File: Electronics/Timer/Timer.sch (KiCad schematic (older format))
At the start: 24 parts, among them J1 RJ10, U1 MIC5504-3.3YM5, U2 74HC165

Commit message: Updated boards for two-sided manufacture.
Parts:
- C1, C2, C3, C4, C5: symbol Device:C -> Timer-rescue:C-Device
- D1: footprint Diodes_SMD:D_SOD-123 -> Diode_SMD:D_SMA_Handsoldering; symbol Device:D_Schottky -> Timer-rescue:D_Schottky-Device
- D2: symbol Device:LED -> Timer-rescue:LED-Device
- D3, D4: symbol Device:D_Zener -> Timer-rescue:D_Zener-Device
- J1: symbol Connector:RJ10 -> Timer-rescue:RJ10-Connector
- R1, R2, R3, R4, R5, R6: symbol Device:R -> Timer-rescue:R-Device
- RN1: symbol Device:R_Network05 -> Timer-rescue:R_Network05-Device
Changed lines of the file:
@@
 EESchema Schematic File Version 4
-LIBS:Timer-cache
-EELAYER 26 0
+EELAYER 30 0
 EELAYER END
 $Descr A4 11693 8268
@@
 $EndDescr
 $Comp
-L power:GND #PWR01
+L Timer-rescue:GND-power #PWR01
 U 1 1 5B2D833C
 P 1450 1550
@@
 $EndComp
 $Comp
-L power:PWR_FLAG #FLG02
+L Timer-rescue:PWR_FLAG-power #FLG02
 U 1 1 5B2D8350
 P 1450 1500
@@
 $EndComp
 $Comp
-L Device:R_Network05 RN1
+L Timer-rescue:R_Network05-Device RN1
 U 1 1 5B2D83AE
 P 9100 1100
@@
 $EndComp
 $Comp
-L Device:LED D2
+L Timer-rescue:LED-Device D2
 U 1 1 5B2D9078
 P 3600 3700
@@
 $EndComp
 $Comp
-L power:+3.3V #PWR03
+L Timer-rescue:+3.3V-power #PWR03
 U 1 1 5B2D91A7
 P 6300 3700
@@
 $EndComp
 $Comp
-L power:GND #PWR04
+L Timer-rescue:GND-power #PWR04
 U 1 1 5B2D939C
 P 2000 3600
@@
 NoConn ~ 8300 1550
 $Comp
-L power:GND #PWR05
+L Timer-rescue:GND-power #PWR05
 U 1 1 5B2D93FE
 P 7700 3250
@@
 $EndComp
 $Comp
-L Device:C C2
+L Timer-rescue:C-Device C2
 U 1 1 5B2D958C
 P 8000 1000
@@
 $EndComp
 $Comp
-L power:GND #PWR06
+L Timer-rescue:GND-power #PWR06
 U 1 1 5B2D95FE
 P 8150 1000
@@
 $EndComp
 $Comp
-L power:+3.3V #PWR07
+L Timer-rescue:+3.3V-power #PWR07
 U 1 1 5B2D9621
 P 7700 950
@@
 NoConn ~ 10400 5350
 $Comp
-L power:GND #PWR08
+L Timer-rescue:GND-power #PWR08
 U 1 1 5B2DA1C3
 P 10400 1950
@@
 $EndComp
 $Comp
-L power:GND #PWR09
+L Timer-rescue:GND-power #PWR09
 U 1 1 5B2DA234
 P 10400 2850
@@
 $EndComp
 $Comp
-L Device:R R1
+L Timer-rescue:R-Device R1
 U 1 1 5B46CBDD
 P 3200 3300
@@
 $EndComp
 $Comp
-L Device:D_Zener D3
+L Timer-rescue:D_Zener-Device D3
 U 1 1 5B46CC66
 P 4250 3600
@@
 $EndComp
 $Comp
-L power:GND #PWR010
+L Timer-rescue:GND-power #PWR010
 U 1 1 5B46CF5B
 P 4250 3850
@@
 $EndComp
 $Comp
-L Device:D_Schottky D1
+L Timer-rescue:D_Schottky-Device D1
 U 1 1 5B5B5DBA
 P 3800 3300
 F 0 "D1" H 3800 3400 50  0000 C CNN
 F 1 "BAT54" H 3800 3200 50  0000 C CNN
-F 2 "Diodes_SMD:D_SOD-123" H 3800 3300 50  0001 C CNN
+F 2 "Diode_SMD:D_SMA_Handsoldering" H 3800 3300 50  0001 C CNN
 F 3 "" H 3800 3300 50  0001 C CNN
 	1    3800 3300
@@
 $EndComp
 $Comp
-L Device:C C1
+L Timer-rescue:C-Device C1
 U 1 1 5B5B6007
 P 4600 3600
@@
 $EndComp
 $Comp
-L Device:R R2
+L Timer-rescue:R-Device R2
 U 1 1 5B5B6D85
 P 3200 3700
@@
 $EndComp
 $Comp
-L power:GND #PWR011
+L Timer-rescue:GND-power #PWR011
 U 1 1 5B5B72D4
 P 6200 4250
@@
 $EndComp
 $Comp
-L power:GND #PWR012
+L Timer-rescue:GND-power #PWR012
 U 1 1 5B5E52E5
 P 4600 3850
@@
 $EndComp
 $Comp
-L power:GND #PWR013
+L Timer-rescue:GND-power #PWR013
 U 1 1 5B5E531A
 P 5350 4250
@@
 $EndComp
 $Comp
-L power:+5V #PWR014
+L Timer-rescue:+5V-power #PWR014
 U 1 1 5B5E5952
 P 5000 3300
@@
 $EndComp
 $Comp
-L power:+5V #PWR015
+L Timer-rescue:+5V-power #PWR015
 U 1 1 5B5E5C2E
 P 5800 3900
@@
 $EndComp
 $Comp
-L Device:D_Zener D4
+L Timer-rescue:D_Zener-Device D4
 U 1 1 5B5E643D
 P 6200 4000
@@
 $EndComp
 $Comp
-L power:GND #PWR016
+L Timer-rescue:GND-power #PWR016
 U 1 1 5B5E67AC
 P 8300 2600
@@
 $EndComp
 $Comp
-L power:GND #PWR018
+L Timer-rescue:GND-power #PWR018
 U 1 1 5B5E6846
 P 7100 1850
@@
 $EndComp
 $Comp
-L power:GND #PWR019
+L Timer-rescue:GND-power #PWR019
 U 1 1 5B5E781E
 P 3850 3700
@@
 $EndComp
 $Comp
-L Device:R R3
+L Timer-rescue:R-Device R3
 U 1 1 5B5E7B1D
 P 3200 4100
@@
 CLK
 $Comp
-L Device:C C3
+L Timer-rescue:C-Device C3
 U 1 1 5B5E8ED0
 P 2400 4400
@@
 $EndComp
 $Comp
-L power:GND #PWR020
+L Timer-rescue:GND-power #PWR020
 U 1 1 5B5E8FC7
 P 2400 4650
@@
 Q
 $Comp
-L Device:R R4
+L Timer-rescue:R-Device R4
 U 1 1 5B5E9AEB
 P 3200 4500
@@
 $EndComp
 $Comp
-L Device:R R5
+L Timer-rescue:R-Device R5
 U 1 1 5B5E9B57
 P 2050 4100
@@
 CLK
 $Comp
-L power:GND #PWR021
+L Timer-rescue:GND-power #PWR021
 U 1 1 5B5EA020
 P 7100 2900
@@
 $EndComp
 $Comp
-L power:GND #PWR022
+L Timer-rescue:GND-power #PWR022
 U 1 1 5B5EA568
 P 10400 3750
@@
 $EndComp
 $Comp
-L power:GND #PWR023
+L Timer-rescue:GND-power #PWR023
 U 1 1 5B5EA5B2
 P 10400 4650
@@
 $EndComp
 $Comp
-L power:GND #PWR024
+L Timer-rescue:GND-power #PWR024
 U 1 1 5B5EA5FC
 P 10400 5550
@@
 $EndComp
 $Comp
-L power:+3.3V #PWR025
+L Timer-rescue:+3.3V-power #PWR025
 U 1 1 5B5E2650
 P 8300 2450
@@
 NoConn ~ 9300 1300
 $Comp
-L Device:R R6
+L Timer-rescue:R-Device R6
 U 1 1 5B5E2B7E
 P 8800 2750
@@
 $EndComp
 $Comp
-L power:+3.3V #PWR026
+L Timer-rescue:+3.3V-power #PWR026
 U 1 1 5B5E2F61
 P 8800 2600
@@
 	9300 4550 8900 4550
 $Comp
-L power:+3.3V #PWR0101
+L Timer-rescue:+3.3V-power #PWR0101
 U 1 1 5B5E304C
 P 8900 900
@@
 	9200 1850 9300 1850
 $Comp
-L power:GND #PWR0102
+L Timer-rescue:GND-power #PWR0102
 U 1 1 5BC0F80F
 P 9300 5000
@@
 $EndComp
 $Comp
-L power:GND #PWR0103
+L Timer-rescue:GND-power #PWR0103
 U 1 1 5BC0F846
 P 9300 5900
@@
 $EndComp
 $Comp
-L power:GND #PWR0104
+L Timer-rescue:GND-power #PWR0104
 U 1 1 5BC0F87D
 P 10400 5100
@@
 $EndComp
 $Comp
-L power:GND #PWR0105
+L Timer-rescue:GND-power #PWR0105
 U 1 1 5BC14F66
 P 10400 4900
@@
 $EndComp
 $Comp
-L power:GND #PWR0106
+L Timer-rescue:GND-power #PWR0106
 U 1 1 5BC17578
 P 10400 5800
@@
 $EndComp
 $Comp
-L power:GND #PWR0107
+L Timer-rescue:GND-power #PWR0107
 U 1 1 5BC175AF
 P 10400 6000
@@
 $EndComp
 $Comp
-L power:GND #PWR0108
+L Timer-rescue:GND-power #PWR0108
 U 1 1 5BC1AEE3
 P 9300 4100
@@
 $EndComp
 $Comp
-L power:GND #PWR0109
+L Timer-rescue:GND-power #PWR0109
 U 1 1 5BC1AF1A
 P 10400 4200
@@
 $EndComp
 $Comp
-L power:GND #PWR0110
+L Timer-rescue:GND-power #PWR0110
 U 1 1 5BC1AF51
 P 10400 4000
@@
 $EndComp
 $Comp
-L power:GND #PWR0111
+L Timer-rescue:GND-power #PWR0111
 U 1 1 5BC1E4A7
 P 10400 3100
@@
 $EndComp
 $Comp
-L power:GND #PWR0112
+L Timer-rescue:GND-power #PWR0112
 U 1 1 5BC1E4DE
 P 10400 3300
@@
 $EndComp
 $Comp
-L power:GND #PWR0113
+L Timer-rescue:GND-power #PWR0113
 U 1 1 5BC1E515
 P 9300 3200
@@
 $EndComp
 $Comp
-L power:GND #PWR0114
+L Timer-rescue:GND-power #PWR0114
 U 1 1 5BC21A81
 P 9300 2300
@@
 $EndComp
 $Comp
-L power:GND #PWR0115
+L Timer-rescue:GND-power #PWR0115
 U 1 1 5BC21AB8
 P 10400 2200
@@
 $EndComp
 $Comp
-L power:GND #PWR0116
+L Timer-rescue:GND-power #PWR0116
 U 1 1 5BC21AEF
 P 10400 2400
@@
 $EndComp
 $Comp
-L Device:C C4
+L Timer-rescue:C-Device C4
 U 1 1 5C3BCA70
 P 6150 1550
@@
 	6150 1400 7100 1400
 $Comp
-L power:GND #PWR0117
+L Timer-rescue:GND-power #PWR0117
 U 1 1 5C3BDD23
 P 6150 1700
@@
 $EndComp
 $Comp
-L Device:C C5
+L Timer-rescue:C-Device C5
 U 1 1 5C3C02A8
 P 6550 1700
@@
 $EndComp
 $Comp
-L power:GND #PWR0118
+L Timer-rescue:GND-power #PWR0118
 U 1 1 5C3C02AF
 P 6550 1850
@@
 	6550 1550 7100 1550
 $Comp
-L Connector:RJ10 J1
+L Timer-rescue:RJ10-Connector J1
 U 1 1 5C3D5B2C
 P 1600 3500
@@
 	8300 2900 8800 2900
 $Comp
-L power:GND #PWR017
+L Timer-rescue:GND-power #PWR017
 U 1 1 5B5E67F9
 P 8300 2750

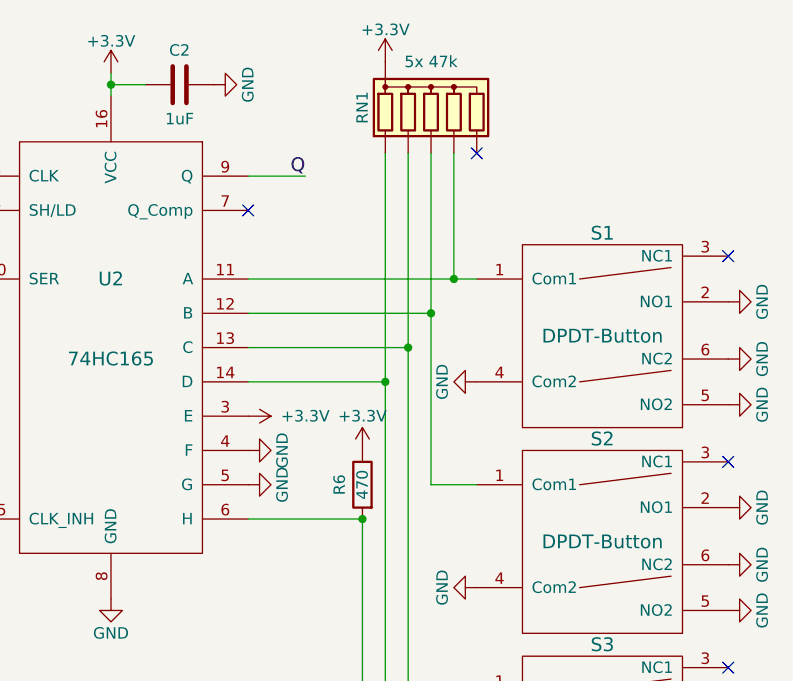
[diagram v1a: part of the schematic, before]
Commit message: Updated component sourcing
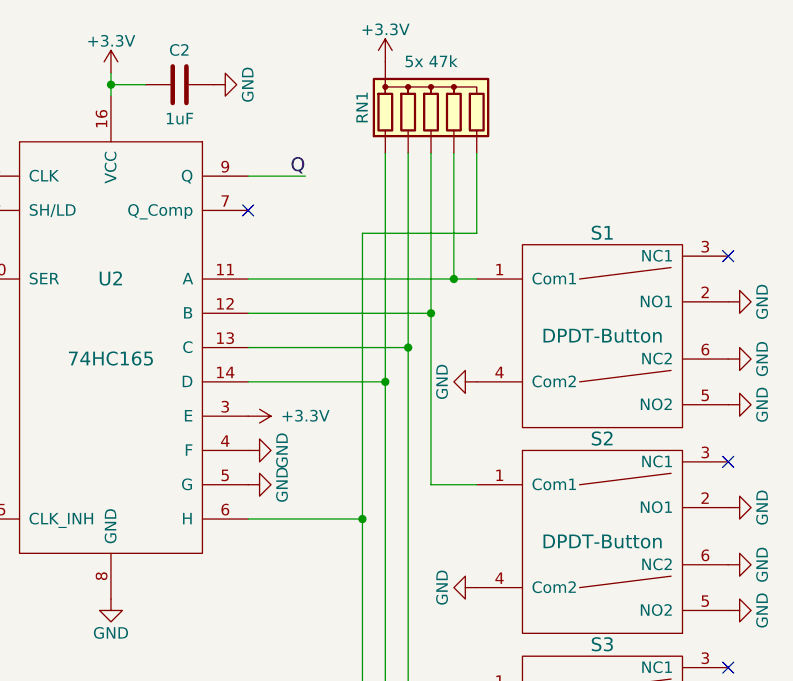
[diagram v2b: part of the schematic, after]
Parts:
- removed R6: 470, Resistors_SMD:R_1206_HandSoldering, symbol Timer-rescue:R-Device
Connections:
- net at RN1.6 (R5): now also S5.1 (Com1), U2.6 (H)
- no-connect marks 7 -> 6
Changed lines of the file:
@@
 Wire Wire Line
 	8800 5450 9300 5450
-NoConn ~ 9300 1300
-$Comp
-L Timer-rescue:R-Device R6
-U 1 1 5B5E2B7E
-P 8800 2750
-F 0 "R6" V 8900 2750 50  0000 C CNN
-F 1 "470" V 8800 2750 50  0000 C CNN
-F 2 "Resistors_SMD:R_1206_HandSoldering" V 8730 2750 50  0001 C CNN
-F 3 "" H 8800 2750 50  0001 C CNN
-	1    8800 2750
-	-1   0    0    -1
-$EndComp
-$Comp
-L Timer-rescue:+3.3V-power #PWR026
-U 1 1 5B5E2F61
-P 8800 2600
-F 0 "#PWR026" H 8800 2450 50  0001 C CNN
-F 1 "+3.3V" H 8800 2750 50  0000 C CNN
-F 2 "" H 8800 2600 50  0001 C CNN
-F 3 "" H 8800 2600 50  0001 C CNN
-	1    8800 2600
-	-1   0    0    -1
-$EndComp
 Wire Wire Line
 	9300 4550 8900 4550
@@
 Wire Wire Line
 	8900 2300 8300 2300
-Connection ~ 8800 2900
 Wire Wire Line
 	8300 2900 8800 2900
@@
 	0    -1   1    0
 $EndComp
+Wire Wire Line
+	8800 2900 8800 1650
+Wire Wire Line
+	8800 1650 9300 1650
+Wire Wire Line
+	9300 1650 9300 1300
+Connection ~ 8800 2900
 $EndSCHEMATC
